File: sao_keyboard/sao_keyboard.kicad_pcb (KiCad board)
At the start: 2 copper layers, 96 x 33 mm, 59 parts, among them J4 I2C, J5 I2C, J6 sao_v2_addon_tht, U1 74LS245, U2 74LS245, U3 74LS245, U4 74LS245, U5 74LS245, U6 CH32V003F4P6, U7 24LC00

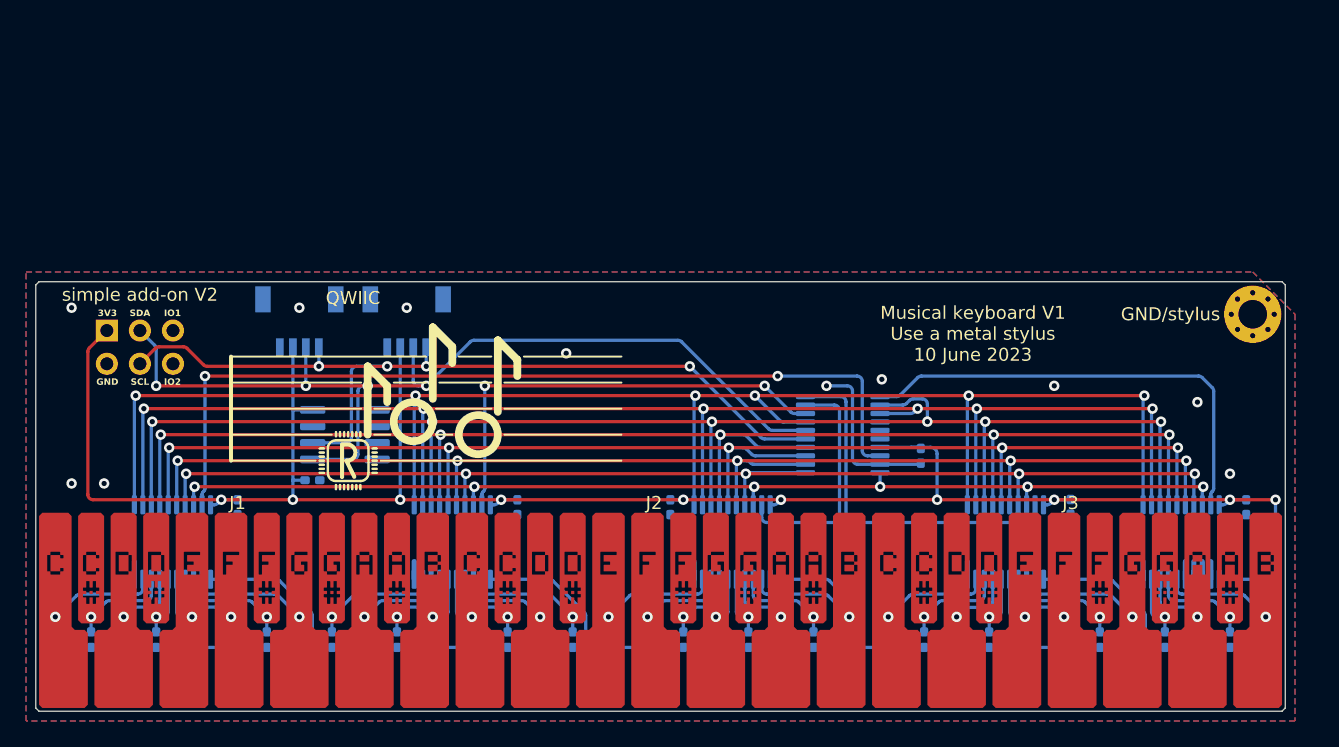
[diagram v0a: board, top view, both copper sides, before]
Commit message: Add some lights to the keyboard addon.
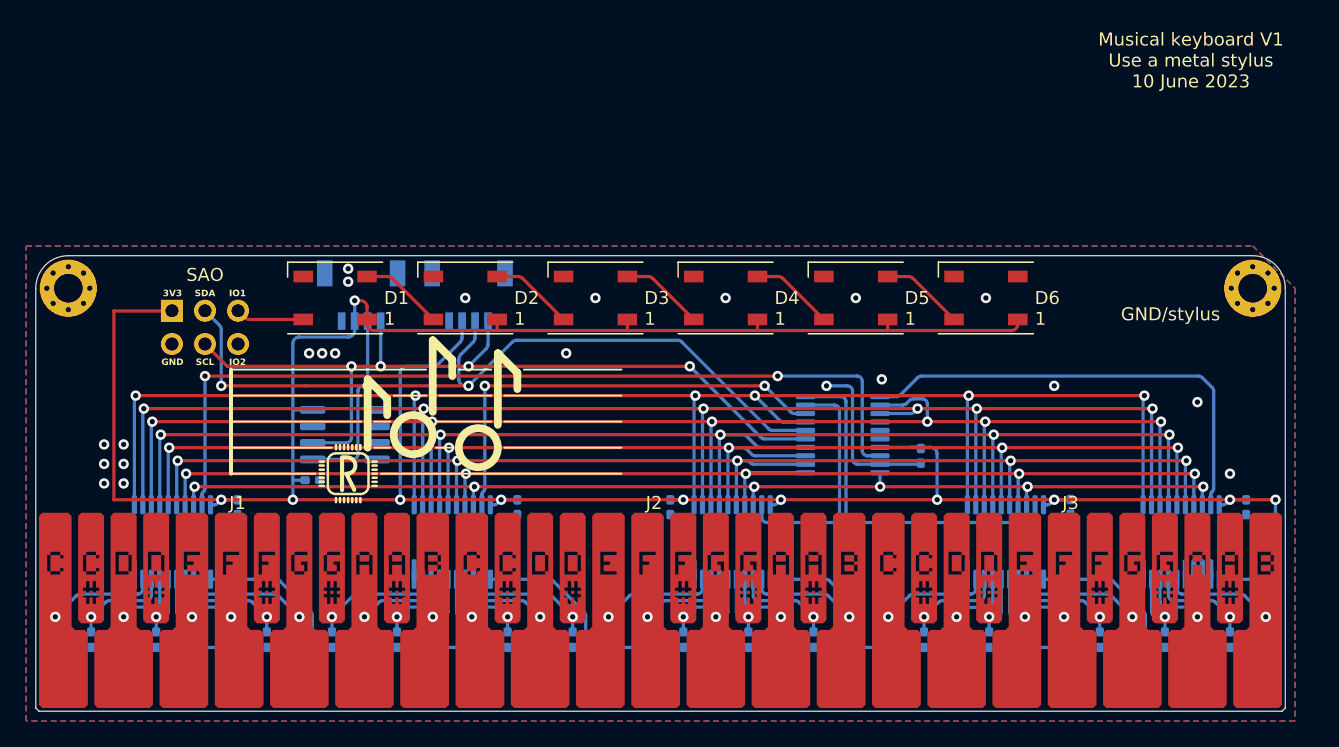
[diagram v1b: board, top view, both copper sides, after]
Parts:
- added D1: WS2812B, LED_SMD:LED_WS2812B_PLCC4_5.0x5.0mm_P3.2mm, F.Cu at (115.2, 70.0)
- added D2: WS2812B, LED_SMD:LED_WS2812B_PLCC4_5.0x5.0mm_P3.2mm, F.Cu at (125.2, 70.0)
- added D3: WS2812B, LED_SMD:LED_WS2812B_PLCC4_5.0x5.0mm_P3.2mm, F.Cu at (135.2, 70.0)
- added D4: WS2812B, LED_SMD:LED_WS2812B_PLCC4_5.0x5.0mm_P3.2mm, F.Cu at (145.2, 70.0)
- added D5: WS2812B, LED_SMD:LED_WS2812B_PLCC4_5.0x5.0mm_P3.2mm, F.Cu at (155.2, 70.0)
- added D6: WS2812B, LED_SMD:LED_WS2812B_PLCC4_5.0x5.0mm_P3.2mm, F.Cu at (165.2, 70.0)
- added H2: MountingHole_Pad, MountingHole:MountingHole_2.2mm_M2_Pad_Via, F.Cu at (94.8, 69.2)
- moved J6 5.23 mm to (105.2, 72.2)
- moved J4 5.15 mm to (117.2, 71.8)
- moved J5 5.15 mm to (125.5, 71.8)
- moved H1 2.00 mm to (185.8, 69.2)
- moved REF** 1.00 mm to (116.2, 83.5)
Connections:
- J6 pad 5: unconnected-(J6-IO1-Pad5) -> LED_DIN
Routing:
- net +3V3: track 304.3 -> 377.8 mm, vias 10 -> 11
- net Net-(D5-DOUT): track 0.00 -> 6.44 mm
- net Net-(D4-DOUT): track 0.00 -> 6.44 mm
- net Net-(D3-DOUT): track 0.00 -> 6.44 mm
- net Net-(D2-DOUT): track 0.00 -> 6.44 mm
- net Net-(D1-DOUT): track 0.00 -> 6.44 mm
- net LED_DIN: track 0.00 -> 5.26 mm
- net SCL: track 68.7 -> 65.3 mm
- net SDA: track 75.2 -> 75.8 mm, vias 4 -> 3
- net GND: vias 11 -> 22
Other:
- board size 96 x 33 mm -> 96 x 35 mm
- board text added: "SAO"
- board text removed: "simple add-on V2"

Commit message: Finish the keyboard design
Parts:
- added R37: 1K, Resistor_SMD:R_0402_1005Metric_Pad0.72x0.64mm_HandSolder, B.Cu at (148.8, 75.0)
- D1, D2, D3, D4, D5, D6: footprint LED_SMD:LED_WS2812B_PLCC4_5.0x5.0mm_P3.2mm -> not_ugly_ws2812b:LED_WS2812B_PLCC4_5.0x5.0mm_P3.2mm
- moved G2 18.0 mm to (134.2, 83.5)
- renumbered REF** to G1, REF** to G2
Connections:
- J6 pad 6: unconnected-(J6-IO2-Pad6) -> SWIO
- U6 pad 18: X1 -> SWIO
- U6 pad 4: unconnected-(U6-PD7-Pad4) -> X1
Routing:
- net SWIO: track 0.00 -> 47.4 mm, vias 0 -> 1
- net X1: track 34.7 -> 54.2 mm
- net +3V3: track 377.8 -> 379.9 mm, vias 11 -> 12
- net GND: vias 22 -> 24
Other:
- board text added: "LED"
- board text added: "Musical keyboard V1 Use a metal stylus 6 July 2023"
- board text added: "SWIO"
- board text removed: "Musical keyboard V1 Use a metal stylus 10 June 2023"
